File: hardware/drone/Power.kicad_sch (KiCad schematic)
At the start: 93 parts, among them Q1 ISP650P06NM, U1 STM32N645I0, U13 LM5907, U16 LMR51635XFDDCR, U18 TPS2121, U3 TPS628303, U4 TPS7A2118PQWDSGRQ1, U5 TPS628303

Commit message: Finished power budget - worst case table
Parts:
- added C123: 100n, symbol Device:C
- added C124: 1u, symbol Device:C
- added TP6, TP7: TestPoint, symbol Connector:TestPoint
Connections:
- net GND: now also C109.2, C110.2, C111.2, C112.2, C113.2, C115.2, C123.2, C124.2; no longer U1.A4 (VDD33USB), U1.D4 (VDDA18USB)
- net VDD2V75: now also TP7.1
- net VDD3V3: now also U1.A4 (VDD33USB), C124.1
- net VDDA1V8: now also U1.D4 (VDDA18USB), C123.1, TP6.1
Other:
- moved on the sheet: C106, C107, C108, C109, C110, C111, C112, C113, C115, C17, C18, C80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

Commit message: Started footprint assignments
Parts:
- C97, C98: footprint Connector:Tag-Connect_TC2030-IDC-FP_2x03_P1.27mm_Vertical -> (none)
- D1, D2: footprint Package_DIP:DIP-40_W15.24mm -> (none)
- Q1: footprint Package_DIP:DIP-24_W7.62mm -> Package_TO_SOT_SMD:SOT-223
- TP1, TP2, TP3, TP4, TP5, TP6, TP7: footprint (none) -> TestPoint:TestPoint_Pad_2.0x2.0mm
- U16: footprint Package_TO_SOT_SMD:SOT-23-6 -> (none)
- U18: footprint Package_TO_SOT_SMD:SOT-583-8 -> (none)
- U3, U5: footprint Package_SON:Texas_VSON-HR-8_1.5x2mm_P0.5mm -> TPS628303ARZER:WQFN-HR8_RZE_TEX
- U4: footprint Package_SON:Texas_X2SON-4_1x1mm_P0.65mm -> Package_SON:Texas_DSG0008A_WSON-8-1EP_2x2mm_P0.5mm_EP0.9x1.6mm
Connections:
- net GND: now also U4.9 (GND)
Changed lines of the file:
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@@
 	)
 	(junction
+		(at 69.85 257.81)
+		(diameter 0)
+		(color 0 0 0 0)
+	)
+	(junction
 		(at 113.03 180.34)
 		(diameter 0)
@@
 	(wire
 		(pts
+			(xy 72.39 256.54) (xy 72.39 257.81)
+		)
+		(stroke
+			(width 0)
+			(type default)
+		)
+	)
+	(wire
+		(pts
 			(xy 154.94 252.73) (xy 154.94 254)
 		)
@@
 	(wire
 		(pts
-			(xy 71.12 256.54) (xy 71.12 257.81)
+			(xy 69.85 256.54) (xy 69.85 257.81)
 		)
 		(stroke
@@
 	(wire
 		(pts
+			(xy 69.85 259.08) (xy 69.85 257.81)
+		)
+		(stroke
+			(width 0)
+			(type default)
+		)
+	)
+	(wire
+		(pts
 			(xy 306.07 67.31) (xy 292.1 67.31)
 		)
@@
 	(wire
 		(pts
+			(xy 72.39 257.81) (xy 69.85 257.81)
+		)
+		(stroke
+			(width 0)
+			(type default)
+		)
+	)
+	(wire
+		(pts
 			(xy 212.09 179.07) (xy 212.09 181.61)
 		)
@@
 			)
 		)
-		(property "Footprint" "Package_TO_SOT_SMD:SOT-583-8"
+		(property "Footprint" ""
 			(at 339.09 64.77 0)
 			(hide yes)
@@
 			)
 		)
-		(property "Footprint" ""
+		(property "Footprint" "TestPoint:TestPoint_Pad_2.0x2.0mm"
 			(at 142.24 125.73 0)
 			(hide yes)
@@
 			)
 		)
-		(property "Footprint" ""
+		(property "Footprint" "TestPoint:TestPoint_Pad_2.0x2.0mm"
 			(at 96.52 246.38 0)
 			(hide yes)
@@
 			)
 		)
-		(property "Footprint" ""
+		(property "Footprint" "TestPoint:TestPoint_Pad_2.0x2.0mm"
 			(at 177.8 246.38 0)
 			(hide yes)
@@
 			)
 		)
-		(property "Footprint" ""
+		(property "Footprint" "TestPoint:TestPoint_Pad_2.0x2.0mm"
 			(at 43.18 190.5 0)
 			(hide yes)
@@
 			)
 		)
-		(property "Footprint" ""
+		(property "Footprint" "TestPoint:TestPoint_Pad_2.0x2.0mm"
 			(at 142.24 185.42 0)
 			(hide yes)
@@
 			)
 		)
-		(property "Footprint" "Connector:Tag-Connect_TC2030-IDC-FP_2x03_P1.27mm_Vertical"
+		(property "Footprint" ""
 			(at 373.0752 241.3 0)
 			(hide yes)
@@
 			)
 		)
-		(property "Footprint" "Package_SON:Texas_VSON-HR-8_1.5x2mm_P0.5mm"
+		(property "Footprint" "TPS628303ARZER:WQFN-HR8_RZE_TEX"
 			(at 83.82 127 0)
 			(hide yes)
@@
 			)
 		)
-		(property "Footprint" ""
+		(property "Footprint" "TestPoint:TestPoint_Pad_2.0x2.0mm"
 			(at 143.51 71.12 0)
 			(hide yes)
@@
 			)
 		)
-		(property "Footprint" "Package_TO_SOT_SMD:SOT-23-6"
+		(property "Footprint" ""
 			(at 81.915 66.04 0)
 			(hide yes)
@@
 			)
 		)
-		(property "Footprint" "Package_DIP:DIP-40_W15.24mm"
+		(property "Footprint" ""
 			(at 224.79 66.04 0)
 			(hide yes)
@@
 	(symbol
 		(lib_id "power:GND")
-		(at 71.12 257.81 0)
+		(at 69.85 259.08 0)
 		(unit 1)
 		(body_style 1)
@@
 		(fields_autoplaced yes)
 		(property "Reference" "#PWR027"
-			(at 71.12 264.16 0)
+			(at 69.85 265.43 0)
 			(hide yes)
 			(show_name no)
@@
 		)
 		(property "Value" "GND"
-			(at 71.12 262.89 0)
+			(at 69.85 264.16 0)
 			(show_name no)
 			(do_not_autoplace no)
@@
 		)
 		(property "Footprint" ""
-			(at 71.12 257.81 0)
+			(at 69.85 259.08 0)
 			(hide yes)
 			(show_name no)
@@
 		)
 		(property "Datasheet" ""
-			(at 71.12 257.81 0)
+			(at 69.85 259.08 0)
 			(hide yes)
 			(show_name no)
@@
 		)
 		(property "Description" "Power symbol creates a global label with name \"GND\" , ground"
-			(at 71.12 257.81 0)
+			(at 69.85 259.08 0)
 			(hide yes)
 			(show_name no)
@@
 			)
 		)
-		(property "Footprint" "Package_DIP:DIP-40_W15.24mm"
+		(property "Footprint" ""
 			(at 210.82 66.04 0)
 			(hide yes)
@@
 			)
 		)
-		(property "Footprint" "Connector:Tag-Connect_TC2030-IDC-FP_2x03_P1.27mm_Vertical"
+		(property "Footprint" ""
 			(at 361.6452 241.3 0)
 			(hide yes)
@@
 			)
 		)
-		(property "Footprint" "Package_DIP:DIP-24_W7.62mm"
+		(property "Footprint" "Package_TO_SOT_SMD:SOT-223"
 			(at 196.85 57.15 0)
 			(hide yes)
@@
 			)
 		)
-		(property "Footprint" "Package_SON:Texas_VSON-HR-8_1.5x2mm_P0.5mm"
+		(property "Footprint" "TPS628303ARZER:WQFN-HR8_RZE_TEX"
 			(at 83.82 186.69 0)
 			(hide yes)
@@
 			)
 		)
-		(property "Footprint" ""
+		(property "Footprint" "TestPoint:TestPoint_Pad_2.0x2.0mm"
 			(at 41.91 130.81 0)
 			(hide yes)
@@
 			)
 		)
-		(property "Footprint" "Package_SON:Texas_X2SON-4_1x1mm_P0.65mm"
+		(property "Footprint" "Package_SON:Texas_DSG0008A_WSON-8-1EP_2x2mm_P0.5mm_EP0.9x1.6mm"
 			(at 71.12 245.11 0)
 			(hide yes)
@@
 		(pin "8"
 		)
+		(pin "9"
+		)
 		(instances

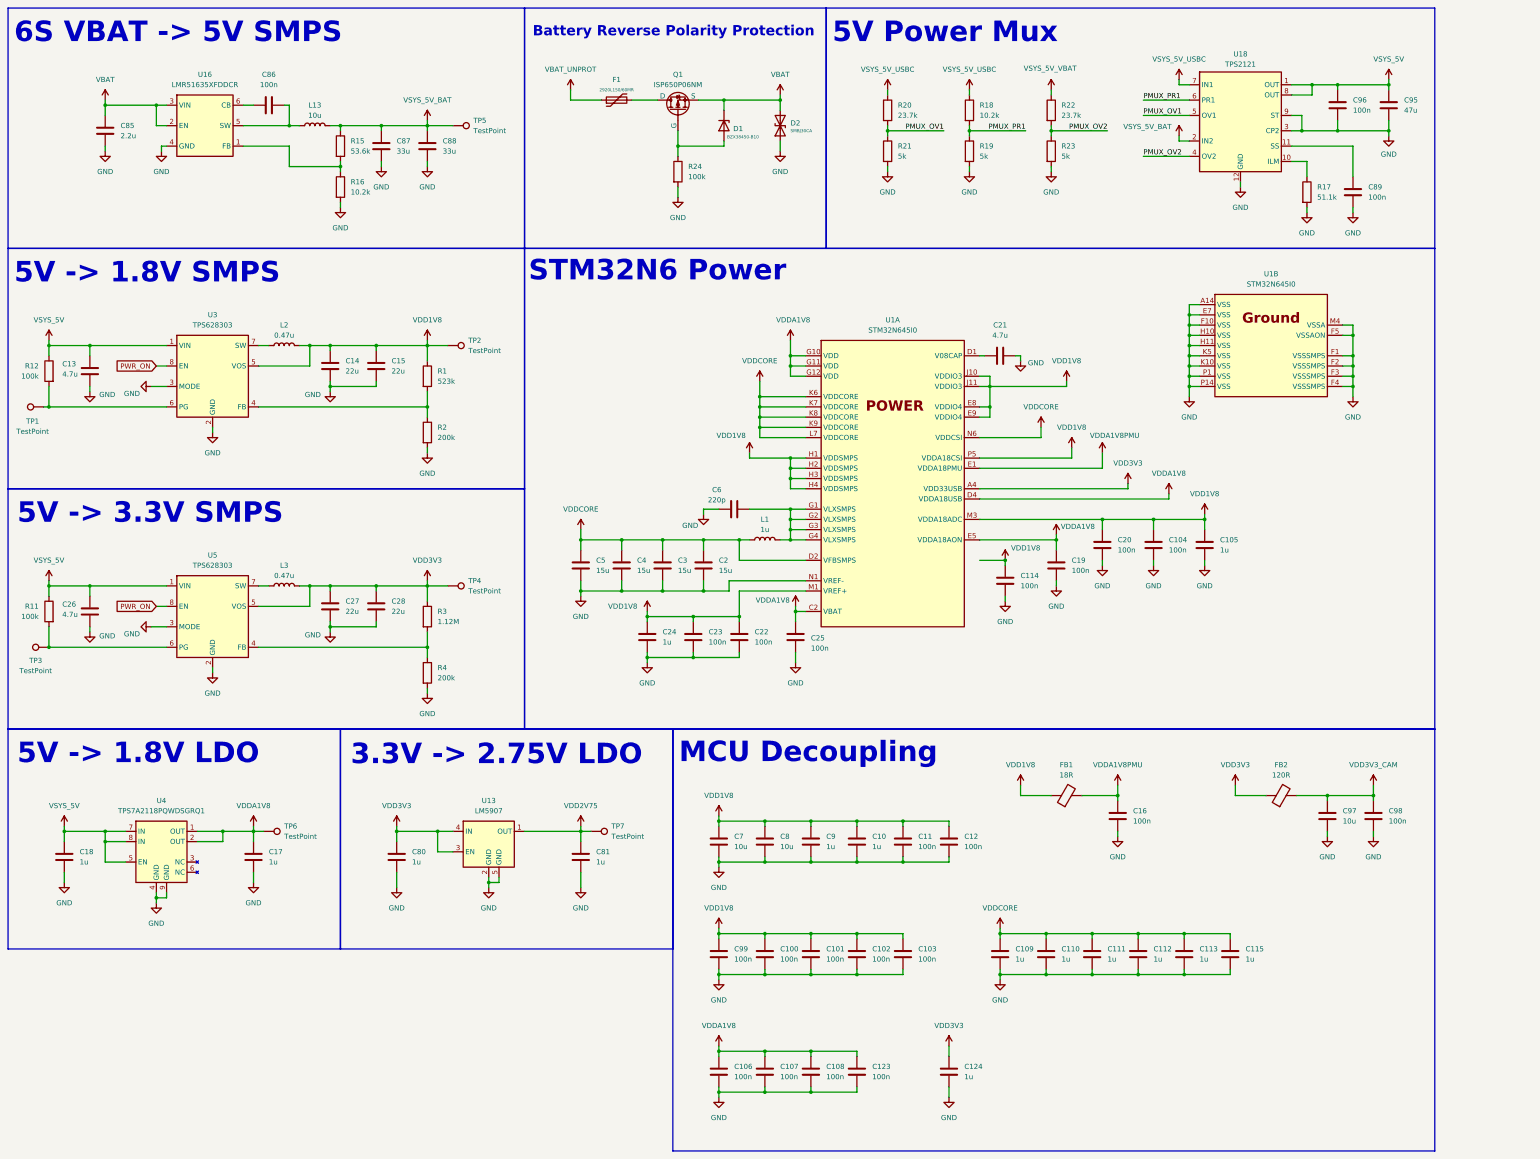
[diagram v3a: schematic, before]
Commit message: Continued footprint assignments
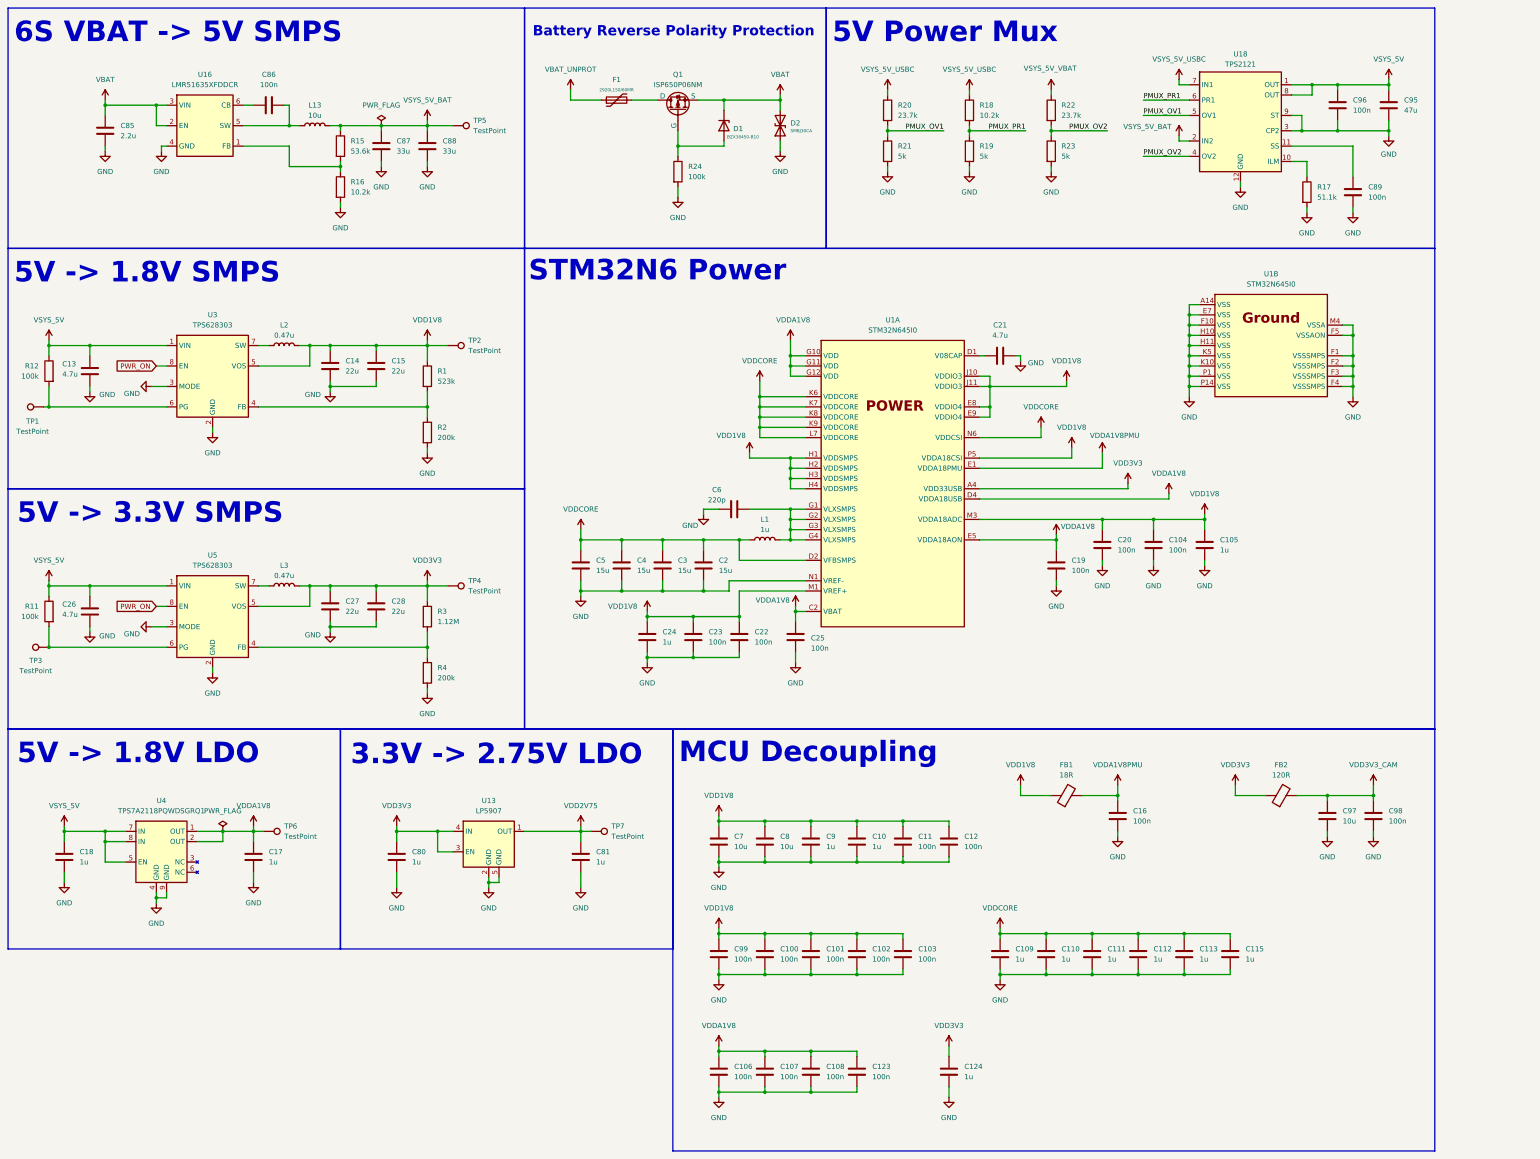
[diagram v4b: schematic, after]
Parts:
- removed C114: 100n, symbol Device:C
- U13: value LM5907 -> LP5907; footprint (none) -> LP5907A28YKMR:BGA4C35P2X2_64X64X50
- U16: footprint (none) -> Package_TO_SOT_SMD:SOT-23-6
- U18: footprint (none) -> TPS2121RUXT:TPS2121RUXT
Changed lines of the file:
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@@
 	)
 	(junction
-		(at 280.67 173.99)
-		(diameter 0)
-		(color 0 0 0 0)
-	)
-	(junction
 		(at 375.92 67.31)
 		(diameter 0)
@@
 	(wire
 		(pts
-			(xy 274.32 173.99) (xy 280.67 173.99)
-		)
-		(stroke
-			(width 0)
-			(type default)
-		)
-	)
-	(wire
-		(pts
 			(xy 351.79 55.88) (xy 356.87 55.88)
 		)
@@
 	(wire
 		(pts
-			(xy 280.67 182.88) (xy 280.67 184.15)
-		)
-		(stroke
-			(width 0)
-			(type default)
-		)
-	)
-	(wire
-		(pts
 			(xy 313.69 266.7) (xy 302.26 266.7)
 		)
@@
 	(wire
 		(pts
-			(xy 280.67 173.99) (xy 280.67 175.26)
-		)
-		(stroke
-			(width 0)
-			(type default)
-		)
-	)
-	(wire
-		(pts
 			(xy 137.16 184.15) (xy 137.16 180.34)
 		)
@@
 			)
 		)
-		(property "Footprint" ""
+		(property "Footprint" "TPS2121RUXT:TPS2121RUXT"
 			(at 339.09 64.77 0)
 			(hide yes)
@@
 	)
 	(symbol
+		(lib_id "power:PWR_FLAG")
+		(at 86.36 241.3 0)
+		(unit 1)
+		(body_style 1)
+		(exclude_from_sim no)
+		(in_bom yes)
+		(on_board yes)
+		(in_pos_files yes)
+		(dnp no)
+		(fields_autoplaced yes)
+		(property "Reference" "#FLG02"
+			(at 86.36 239.395 0)
+			(hide yes)
+			(show_name no)
+			(do_not_autoplace no)
+			(effects
+				(font
+					(size 1.27 1.27)
+				)
+			)
+		)
+		(property "Value" "PWR_FLAG"
+			(at 86.36 236.22 0)
+			(show_name no)
+			(do_not_autoplace no)
+			(effects
+				(font
+					(size 1.27 1.27)
+				)
+			)
+		)
+		(property "Footprint" ""
+			(at 86.36 241.3 0)
+			(hide yes)
+			(show_name no)
+			(do_not_autoplace no)
+			(effects
+				(font
+					(size 1.27 1.27)
+				)
+			)
+		)
+		(property "Datasheet" ""
+			(at 86.36 241.3 0)
+			(hide yes)
+			(show_name no)
+			(do_not_autoplace no)
+			(effects
+				(font
+					(size 1.27 1.27)
+				)
+			)
+		)
+		(property "Description" "Special symbol for telling ERC where power comes from"
+			(at 86.36 241.3 0)
+			(hide yes)
+			(show_name no)
+			(do_not_autoplace no)
+			(effects
+				(font
+					(size 1.27 1.27)
+				)
+			)
+		)
+		(pin "1"
+		)
+		(instances
+			(project "drone"
+				(path "/62c402a6-ed3f-446b-8423-821e9cc6908b/9b1c1f9e-2215-43f5-a9f4-c7f468848b2f"
+					(reference "#FLG02")
+					(unit 1)
+				)
+			)
+		)
+	)
+	(symbol
 		(lib_id "power:VDD")
 		(at 271.78 57.15 0)
@@
 	)
 	(symbol
+		(lib_id "power:PWR_FLAG")
+		(at 125.73 66.04 0)
+		(unit 1)
+		(body_style 1)
+		(exclude_from_sim no)
+		(in_bom yes)
+		(on_board yes)
+		(in_pos_files yes)
+		(dnp no)
+		(fields_autoplaced yes)
+		(property "Reference" "#FLG03"
+			(at 125.73 64.135 0)
+			(hide yes)
+			(show_name no)
+			(do_not_autoplace no)
+			(effects
+				(font
+					(size 1.27 1.27)
+				)
+			)
+		)
+		(property "Value" "PWR_FLAG"
+			(at 125.73 60.96 0)
+			(show_name no)
+			(do_not_autoplace no)
+			(effects
+				(font
+					(size 1.27 1.27)
+				)
+			)
+		)
+		(property "Footprint" ""
+			(at 125.73 66.04 0)
+			(hide yes)
+			(show_name no)
+			(do_not_autoplace no)
+			(effects
+				(font
+					(size 1.27 1.27)
+				)
+			)
+		)
+		(property "Datasheet" ""
+			(at 125.73 66.04 0)
+			(hide yes)
+			(show_name no)
+			(do_not_autoplace no)
+			(effects
+				(font
+					(size 1.27 1.27)
+				)
+			)
+		)
+		(property "Description" "Special symbol for telling ERC where power comes from"
+			(at 125.73 66.04 0)
+			(hide yes)
+			(show_name no)
+			(do_not_autoplace no)
+			(effects
+				(font
+					(size 1.27 1.27)
+				)
+			)
+		)
+		(pin "1"
+		)
+		(instances
+			(project "drone"
+				(path "/62c402a6-ed3f-446b-8423-821e9cc6908b/9b1c1f9e-2215-43f5-a9f4-c7f468848b2f"
+					(reference "#FLG03")
+					(unit 1)
+				)
+			)
+		)
+	)
+	(symbol
 		(lib_id "power:VDD")
 		(at 293.37 167.64 0)
@@
 			)
 		)
-		(property "Value" "LM5907"
+		(property "Value" "LP5907"
 			(at 152.4 236.22 0)
 			(show_name no)
@@
 			)
 		)
-		(property "Footprint" ""
+		(property "Footprint" "LP5907A28YKMR:BGA4C35P2X2_64X64X50"
 			(at 152.4 245.11 0)
 			(hide yes)
@@
 			)
 		)
-		(property "Footprint" ""
+		(property "Footprint" "Package_TO_SOT_SMD:SOT-23-6"
 			(at 81.915 66.04 0)
 			(hide yes)
@@
 	)
 	(symbol
-		(lib_id "Device:C")
-		(at 280.67 179.07 0)
-		(unit 1)
-		(body_style 1)
-		(exclude_from_sim no)
-		(in_bom yes)
-		(on_board yes)
-		(in_pos_files yes)
-		(dnp no)
-		(fields_autoplaced yes)
-		(property "Reference" "C114"
-			(at 284.48 177.7999 0)
-			(show_name no)
-			(do_not_autoplace no)
-			(effects
-				(font
-					(size 1.27 1.27)
-				)
-				(justify left)
-			)
-		)
-		(property "Value" "100n"
-			(at 284.48 180.3399 0)
-			(show_name no)
-			(do_not_autoplace no)
-			(effects
-				(font
-					(size 1.27 1.27)
-				)
-				(justify left)
-			)
-		)
-		(property "Footprint" ""
-			(at 281.6352 182.88 0)
-			(hide yes)
-			(show_name no)
-			(do_not_autoplace no)
-			(effects
-				(font
-					(size 1.27 1.27)
-				)
-			)
-		)
-		(property "Datasheet" ""
-			(at 280.67 179.07 0)
-			(hide yes)
-			(show_name no)
-			(do_not_autoplace no)
-			(effects
-				(font
-					(size 1.27 1.27)
-				)
-			)
-		)
-		(property "Description" "Unpolarized capacitor"
-			(at 280.67 179.07 0)
-			(hide yes)
-			(show_name no)
-			(do_not_autoplace no)
-			(effects
-				(font
-					(size 1.27 1.27)
-				)
-			)
-		)
-		(pin "2"
-		)
-		(pin "1"
-		)
-		(instances
-			(project "drone"
-				(path "/62c402a6-ed3f-446b-8423-821e9cc6908b/9b1c1f9e-2215-43f5-a9f4-c7f468848b2f"
-					(reference "C114")
-					(unit 1)
-				)
-			)
-		)
-	)
-	(symbol
 		(lib_id "power:GND")
 		(at 293.37 180.34 0)
@@
 					(unit 1)
 				)
-			)
-		)
-	)
-	(symbol
-		(lib_id "power:VDD")
-		(at 280.67 173.99 0)
-		(unit 1)
-		(body_style 1)
-		(exclude_from_sim no)
-		(in_bom yes)
-		(on_board yes)
-		(in_pos_files yes)
-		(dnp no)
-		(property "Reference" "#PWR0180"
-			(at 280.67 177.8 0)
-			(hide yes)
-			(show_name no)
-			(do_not_autoplace no)
-			(effects
-				(font
-					(size 1.27 1.27)
-				)
-			)
-		)
-		(property "Value" "VDD1V8"
-			(at 285.75 170.942 0)
-			(show_name no)
-			(do_not_autoplace no)
-			(effects
-				(font
-					(size 1.27 1.27)
-				)
-			)
-		)
-		(property "Footprint" ""
-			(at 280.67 173.99 0)
-			(hide yes)
-			(show_name no)
-			(do_not_autoplace no)
-			(effects
-				(font
-					(size 1.27 1.27)
-				)
-			)
-		)
-		(property "Datasheet" ""
-			(at 280.67 173.99 0)
-			(hide yes)
-			(show_name no)
-			(do_not_autoplace no)
-			(effects
-				(font
-					(size 1.27 1.27)
-				)
-			)
-		)
-		(property "Description" "Power symbol creates a global label with name \"VDD\""
-			(at 280.67 173.99 0)
-			(hide yes)
-			(show_name no)
-			(do_not_autoplace no)
-			(effects
-				(font
-					(size 1.27 1.27)
-				)
-			)
-		)
-		(pin "1"
-		)
-		(instances
-			(project "drone"
-				(path "/62c402a6-ed3f-446b-8423-821e9cc6908b/9b1c1f9e-2215-43f5-a9f4-c7f468848b2f"
-					(reference "#PWR0180")
-					(unit 1)
-				)
-			)
-		)
-	)
-	(symbol
-		(lib_id "power:GND")
-		(at 280.67 184.15 0)
-		(unit 1)
-		(body_style 1)
-		(exclude_from_sim no)
-		(in_bom yes)
-		(on_board yes)
-		(in_pos_files yes)
-		(dnp no)
-		(fields_autoplaced yes)
-		(property "Reference" "#PWR0181"
-			(at 280.67 190.5 0)
-			(hide yes)
-			(show_name no)
-			(do_not_autoplace no)
-			(effects
-				(font
-					(size 1.27 1.27)
-				)
-			)
-		)
-		(property "Value" "GND"
-			(at 280.67 189.23 0)
-			(show_name no)
-			(do_not_autoplace no)
-			(effects
-				(font
-					(size 1.27 1.27)
-				)
-			)
-		)
-		(property "Footprint" ""
-			(at 280.67 184.15 0)
-			(hide yes)
-			(show_name no)
-			(do_not_autoplace no)
-			(effects
-				(font
-					(size 1.27 1.27)
-				)
-			)
-		)
-		(property "Datasheet" ""
-			(at 280.67 184.15 0)
-			(hide yes)
-			(show_name no)
-			(do_not_autoplace no)
-			(effects
-				(font
-					(size 1.27 1.27)
-				)
-			)
-		)
-		(property "Description" "Power symbol creates a global label with name \"GND\" , ground"
-			(at 280.67 184.15 0)
-			(hide yes)
-			(show_name no)
-			(do_not_autoplace no)
-			(effects
-				(font
-					(size 1.27 1.27)
-				)
-			)
-		)
-		(pin "1"
-		)
-		(instances
-			(project "drone"
-				(path "/62c402a6-ed3f-446b-8423-821e9cc6908b/9b1c1f9e-2215-43f5-a9f4-c7f468848b2f"
-					(reference "#PWR0181")
-					(unit 1)
-				)

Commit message: More footprints
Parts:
- C11, C12, C123, C16, C19, C20, C22, C23, C25: footprint (none) -> Capacitor_SMD:C_0201_0603Metric
- C124: footprint (none) -> Capacitor_SMD:C_0402_1005Metric
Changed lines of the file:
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@@
 			)
 		)
-		(property "Footprint" ""
+		(property "Footprint" "Capacitor_SMD:C_0201_0603Metric"
 			(at 215.5952 196.85 0)
 			(hide yes)
@@
 			)
 		)
-		(property "Footprint" ""
+		(property "Footprint" "Capacitor_SMD:C_0201_0603Metric"
 			(at 244.8052 304.8 0)
 			(hide yes)
@@
 			)
 		)
-		(property "Footprint" ""
+		(property "Footprint" "Capacitor_SMD:C_0201_0603Metric"
 			(at 229.5652 196.85 0)
 			(hide yes)
@@
 			)
 		)
-		(property "Footprint" ""
+		(property "Footprint" "Capacitor_SMD:C_0201_0603Metric"
 			(at 267.6652 247.65 0)
 			(hide yes)
@@
 			)
 		)
-		(property "Footprint" ""
+		(property "Footprint" "Capacitor_SMD:C_0201_0603Metric"
 			(at 305.7652 173.99 0)
 			(hide yes)
@@
 			)
 		)
-		(property "Footprint" ""
+		(property "Footprint" "Capacitor_SMD:C_0201_0603Metric"
 			(at 309.5752 241.3 0)
 			(hide yes)
@@
 			)
 		)
-		(property "Footprint" ""
+		(property "Footprint" "Capacitor_SMD:C_0201_0603Metric"
 			(at 204.1652 196.85 0)
 			(hide yes)
@@
 			)
 		)
-		(property "Footprint" ""
+		(property "Footprint" "Capacitor_SMD:C_0402_1005Metric"
 			(at 267.6652 304.8 0)
 			(hide yes)
@@
 			)
 		)
-		(property "Footprint" ""
+		(property "Footprint" "Capacitor_SMD:C_0201_0603Metric"
 			(at 256.2352 247.65 0)
 			(hide yes)
@@
 			)
 		)
-		(property "Footprint" ""
+		(property "Footprint" "Capacitor_SMD:C_0201_0603Metric"
 			(at 294.3352 179.07 0)
 			(hide yes)
